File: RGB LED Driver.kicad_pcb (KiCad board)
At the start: 2 copper layers, 32 parts, among them J1 UART, J2 LED_STRIP_OUTPUT, J3 5V_POWER_INPUT, J4 PWR_BUTTON_TERMINAL, SW1 FLASH, SW2 MEM_RST, SW3 RESET, U1 ESP-12E, U2 AMS1117-3.3, U3 74LVC2G17

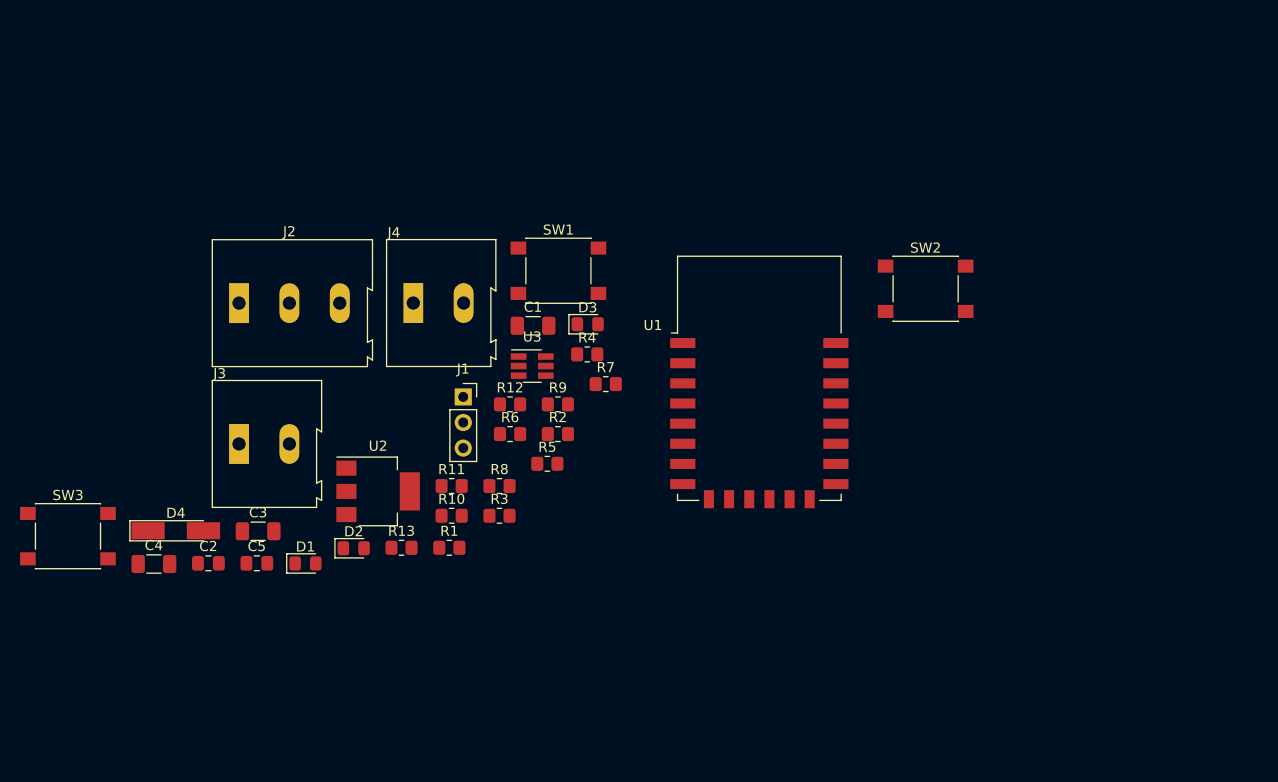
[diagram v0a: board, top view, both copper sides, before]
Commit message: Working on PCB, bad footprint needs to be reworked
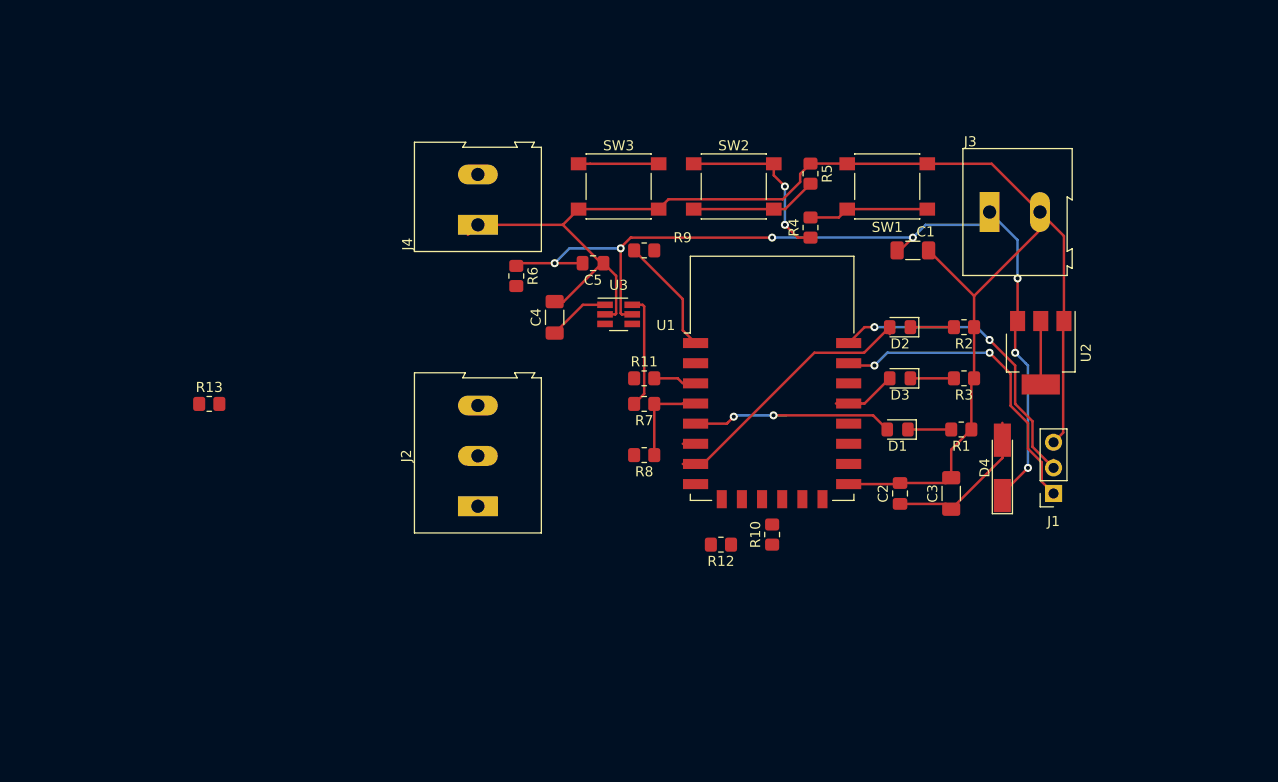
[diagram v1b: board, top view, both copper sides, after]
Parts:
- D1: value WIFI_NOT_CON -> NOT_CON
- D2: value CONNECTING -> CON
- D3: value DUNNO -> STATUS
- D4: value POWER_SUPPLY_DIODE -> PWR_DIODE
- moved D4 82.3 mm to (153.7, 72.4), turned to 90 degrees
- moved J3 78.0 mm to (152.4, 47.0)
- moved C2 69.0 mm to (143.5, 74.9), turned to 90 degrees
- moved C3 68.9 mm to (148.6, 74.9), turned to 90 degrees
- moved U2 67.2 mm to (157.5, 61.0), turned to 270 degrees
- moved SW3 64.8 mm to (115.6, 44.5)
- moved D1 60.3 mm to (143.3, 68.6), turned to 180 degrees
- moved J1 59.4 mm to (158.8, 74.9), turned to 180 degrees
- moved D2 58.5 mm to (143.5, 58.4), turned to 180 degrees
- moved R1 52.2 mm to (149.6, 68.6), turned to 180 degrees
- moved R3 48.1 mm to (149.9, 63.5), turned to 180 degrees
- moved C4 46.7 mm to (109.2, 57.4), turned to 90 degrees
- moved C5 44.7 mm to (113.0, 52.1), turned to 180 degrees
- moved R2 41.7 mm to (149.9, 58.4), turned to 180 degrees
- moved R5 38.9 mm to (134.6, 43.2), turned to 270 degrees
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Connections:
- U1 pad 10: Net-(R12-Pad1) -> Net-(U1-Pad10)
- U1 pad 11: Net-(R10-Pad1) -> Net-(U1-Pad11)
- U1 pad 12: /FLASH_BTN -> Net-(U1-Pad12)
- U1 pad 14: /MEM_RST -> Net-(U1-Pad14)
- U1 pad 15: Net-(J1-Pad1) -> GND
- U1 pad 16: Net-(J1-Pad2) -> Net-(R12-Pad1)
- U1 pad 17: Net-(U1-Pad17) -> Net-(R10-Pad1)
- U1 pad 18: Net-(U1-Pad18) -> /FLASH_BTN
- U1 pad 19: /STATE_LED1 -> /STATE_LED3
- U1 pad 20: Net-(U1-Pad20) -> /MEM_RST
- U1 pad 21: Net-(U1-Pad21) -> Net-(J1-Pad1)
- U1 pad 22: Net-(U1-Pad22) -> Net-(J1-Pad2)
- U1 pad 5: /LED_OUTPUT_PIN -> /STATE_LED1
- U1 pad 6: /STATE_LED2 -> /LED_OUTPUT_PIN
- U1 pad 7: /STATE_LED3 -> /STATE_LED2
- U1 pad 9: GND -> Net-(U1-Pad9)
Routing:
- net GND: track 0.00 -> 152.4 mm
- net +5V: track 0.00 -> 92.6 mm, vias 0 -> 7
- net +3V3: track 0.00 -> 39.8 mm, vias 0 -> 2
- net Net-(J1-Pad2): track 0.00 -> 31.3 mm, vias 0 -> 2
- net Net-(J1-Pad1): track 0.00 -> 31.2 mm, vias 0 -> 2
- net /STATE_LED2: track 0.00 -> 27.1 mm
- net /STATE_LED1: track 0.00 -> 21.6 mm, vias 0 -> 2
- net /RESET: track 0.00 -> 19.7 mm
- net /MEM_RST: track 0.00 -> 12.6 mm
- net /FLASH_BTN: track 0.00 -> 12.1 mm
- net Net-(R7-Pad2): track 0.00 -> 12.1 mm
- net /PWR_BTN: track 0.00 -> 7.93 mm
- net /STATE_LED3: track 0.00 -> 7.63 mm
- net Net-(C4-Pad1): track 0.00 -> 6.16 mm
- net Net-(D3-Pad1): track 0.00 -> 4.33 mm
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
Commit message: Done 1st version of PCB
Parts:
- added REF**: 2.2mm, MountingHole:MountingHole_2.2mm_M2, F.Cu at (94.0, 77.5)
- added REF**: 2.2mm, MountingHole:MountingHole_2.2mm_M2, F.Cu at (163.8, 41.9)
- added REF**: 2.2mm, MountingHole:MountingHole_2.2mm_M2, F.Cu at (94.0, 41.9)
- added REF**: 2.2mm, MountingHole:MountingHole_2.2mm_M2, F.Cu at (163.8, 77.5)
- J4: value PWR_BUTTON_TERMINAL -> PWR_BTN
- SW1: value FLASH -> SW_Push
- SW2: value MEM_RST -> SW_Push
- SW3: value RESET -> SW_Push
- moved R13 37.0 mm to (111.8, 62.2), turned to 90 degrees
- moved R12 22.8 mm to (147.3, 72.7), turned to 90 degrees
- moved R10 13.1 mm to (142.2, 72.7), turned to 270 degrees
- moved R6 10.2 mm to (115.6, 53.3), turned to 180 degrees
- moved R9 9.97 mm to (119.4, 40.9)
- moved J4 6.84 mm to (99.1, 54.6)
- moved J2 5.68 mm to (99.1, 71.1)
- moved C5 4.58 mm to (116.8, 49.5), turned to 0 degrees
- moved SW3 4.02 mm to (111.8, 43.2)
- moved C4 2.54 mm to (111.8, 57.4), turned to 270 degrees
- moved C2 2.54 mm to (143.5, 77.5)
- moved C3 2.54 mm to (148.6, 77.5)
- moved SW1 1.27 mm to (142.2, 43.2)
- moved SW2 1.27 mm to (127.0, 43.2)
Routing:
- net GND: track 152.4 -> 21.6 mm
- net +3V3: track 39.8 -> 134.1 mm, vias 2 -> 8
- net /FLASH_BTN: track 12.1 -> 38.2 mm, vias 0 -> 2
- net /MEM_RST: track 12.6 -> 37.3 mm, vias 0 -> 2
- net Net-(J2-Pad2): track 0.00 -> 23.9 mm, vias 0 -> 1
- net /LED_OUTPUT_PIN: track 1.50 -> 21.0 mm, vias 0 -> 2
- net Net-(J4-Pad2): track 0.00 -> 18.9 mm
- net /RESET: track 19.7 -> 33.5 mm, vias 0 -> 2
- net Net-(R12-Pad1): track 0.00 -> 10.9 mm
- net Net-(C4-Pad1): track 6.16 -> 12.8 mm
- net +5V: track 92.6 -> 98.7 mm, vias 7 -> 5
- net Net-(R10-Pad1): track 0.00 -> 4.52 mm
- net /PWR_BTN: track 7.93 -> 11.8 mm
- net /STATE_LED2: track 27.1 -> 29.6 mm
- net /STATE_LED1: track 21.6 -> 19.5 mm
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- added copper zone on B.Cu, net +5V
- added copper zone on F.Cu, net GND
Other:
- board outline added: 77.5 x 43.2 mm
